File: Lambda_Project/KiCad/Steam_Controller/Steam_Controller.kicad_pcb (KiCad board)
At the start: 2 copper layers, 151 x 77.4 mm, 214 parts, among them J1 MICROQTJ, P1 Conn_ARM_SWD_TagConnect_TC2030, P2 Conn_ARM_SWD_TagConnect_TC2030, P3 781271220, P4 781271220, Q10 DMN2300U-7, Q11 DMN2300U-7, Q12 DMP2035U-7, Q2 DMP2035U-7, Q3 MMBT3906, Q4 DMP2035U-7, Q5 DMP2035U-7, Q6 FDV304P, Q8 FDV304P, U1 LPC11U37FBD64/501,, U10 DMN63D8LDW-7, U2 TPD4E1U06DBVR - NG4P USB, U3 TPS61029DRCR, U4 TLV70230DBVT, U5 NRF51822-QFAB-T, U6 MPU6500, U7 A1304ELHLT-T, U8 A1304ELHLT-T, U9 DMN63D8LDW-7, X1 ABM8-12.000MHZ-B2-T, X2 NX2520SA-16MHZ-STD-CSW-5

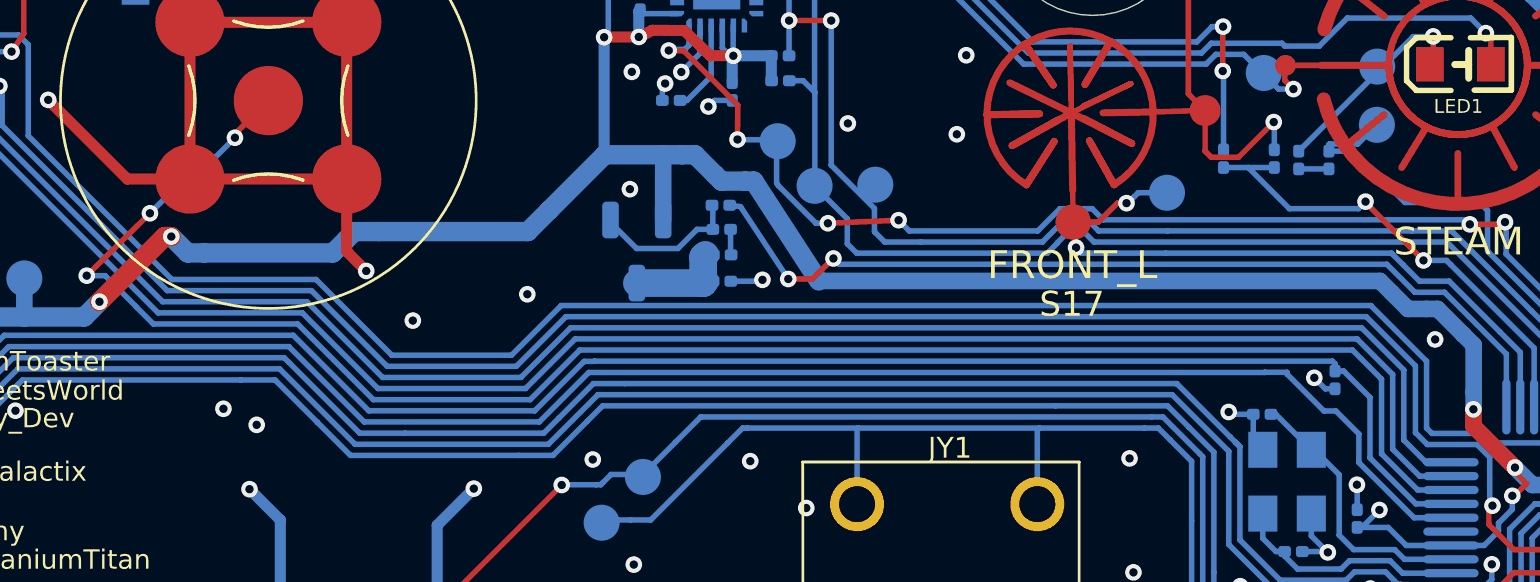
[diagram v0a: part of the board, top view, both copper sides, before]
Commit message: Connect trigger hall effects to power
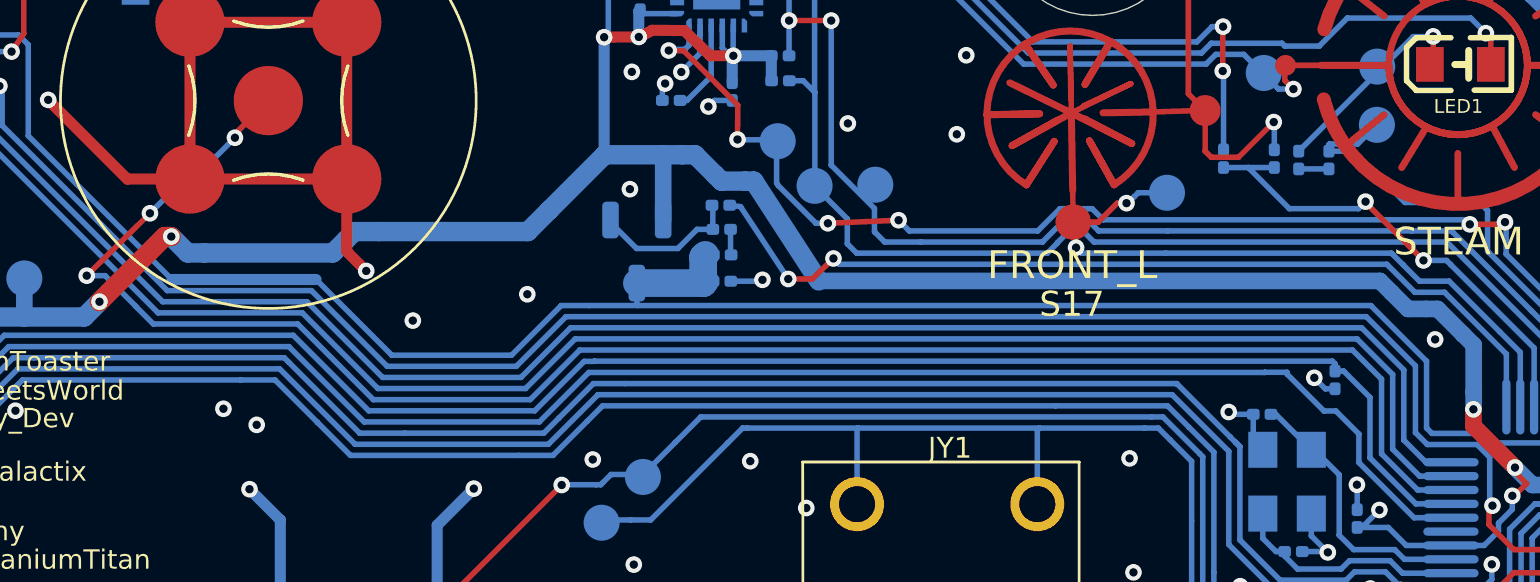
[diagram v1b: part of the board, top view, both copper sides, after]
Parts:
- R18: value 75kΩ -> 27kΩ
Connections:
- R10 pad 2: Net-(R10-Pad2) -> D3-K
- R27 pad 1: Net-(R10-Pad2) -> D3-K
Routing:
- net HAL-VCC: track 152.4 -> 154.1 mm
- net Net-(R10-Pad2): track 1.05 -> 0.00 mm
- net D3-K: track 27.2 -> 28.2 mm
